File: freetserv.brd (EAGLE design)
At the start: 91.4 x 82.5 mm, 72 parts, among them IC2 SN75240PW, Q1 12MHz, Q2 6MHz, U1 MCP16311-E/MS

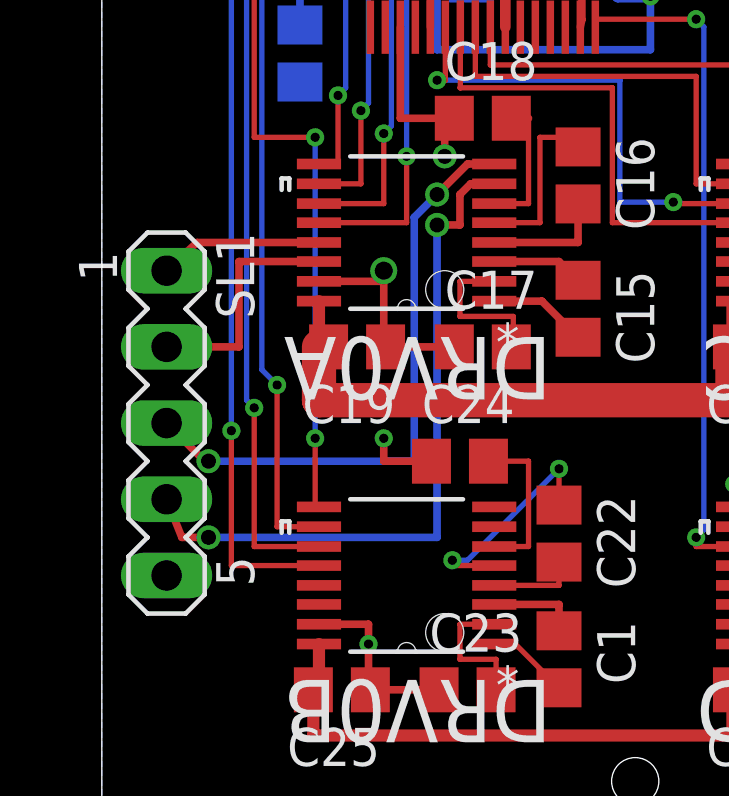
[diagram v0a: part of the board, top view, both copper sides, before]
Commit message: wire up a serial port
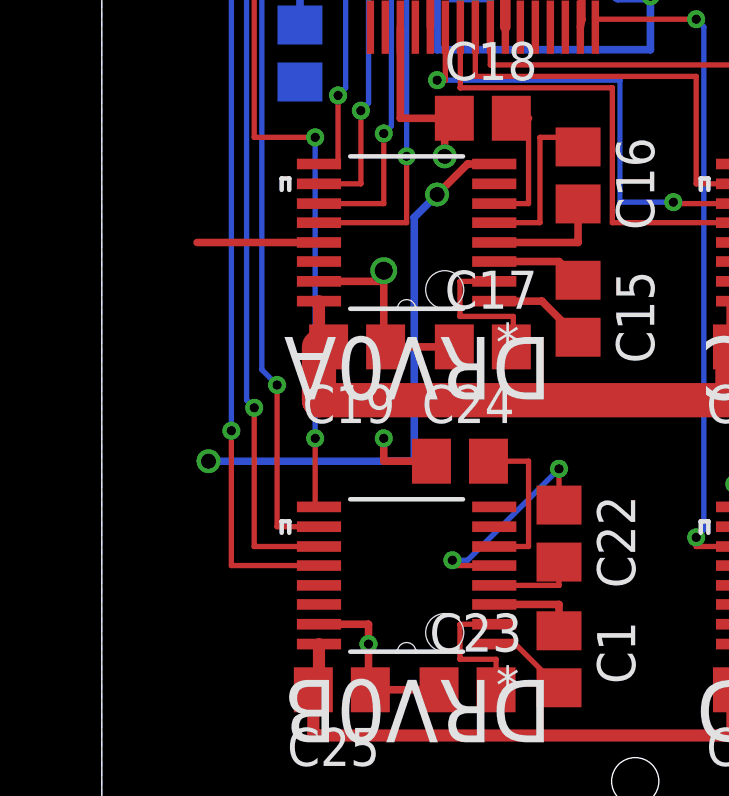
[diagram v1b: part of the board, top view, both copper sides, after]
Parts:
- removed SL1: (no value), con-lstb:MA05-1
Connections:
- removed net N$25: DRV0A.14, SL1.2
- removed net N$8: DRV0A.7, SL1.4
- new net N$37: DRV0A.14
- net GND: no longer SL1.5
- net N$19: no longer SL1.1
- net N$9: no longer SL1.3
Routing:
- net N$8: track 23.4 -> 0.00 mm, vias 2 -> 0
- net N$25: track 7.92 -> 0.00 mm
- net N$9: track 20.3 -> 18.5 mm
- net N$19: track 5.45 -> 4.06 mm
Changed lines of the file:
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@@
 <attribute name="PARTNO" value="1276-1003-1-ND" x="15.875" y="43.815" size="1.778" layer="27" rot="R270" display="off"/>
-</element>
-<element name="SL1" library="con-lstb" package="MA05-1" value="" x="2.159" y="35.56" rot="R270">
-<attribute name="MF" value="" x="2.159" y="35.56" size="1.778" layer="27" rot="R270" display="off"/>
-<attribute name="OC_FARNELL" value="unknown" x="2.159" y="35.56" size="1.778" layer="27" rot="R270" display="off"/>
-<attribute name="OC_NEWARK" value="unknown" x="2.159" y="35.56" size="1.778" layer="27" rot="R270" display="off"/>
-<attribute name="MPN" value="" x="2.159" y="35.56" size="1.778" layer="27" rot="R270" display="off"/>
 </element>
 <element name="C17" library="resistor" package="C0805" value="0.1uF" x="12.7" y="38.1">
@@
 <contactref element="C6" pad="2"/>
 <contactref element="C7" pad="2"/>
-<contactref element="SL1" pad="5"/>
 <polygon width="0.4064" layer="16">
 <vertex x="0" y="82.55"/>
@@
 <signal name="N$19">
 <contactref element="DRV0A" pad="13"/>
-<contactref element="SL1" pad="1"/>
 <wire x1="7.239" y1="41.5798" x2="3.175" y2="41.5798" width="0.254" layer="1"/>
-<wire x1="3.175" y1="41.5798" x2="2.159" y2="40.64" width="0.254" layer="1"/>
 </signal>
 <signal name="+3V3" class="2">
@@
 <wire x1="8.592" y1="57.36" x2="8.636" y2="57.404" width="0.1778" layer="1"/>
 </signal>
-<signal name="N$8">
-<contactref element="DRV0A" pad="7"/>
-<contactref element="SL1" pad="4"/>
-<wire x1="13.081" y1="43.5356" x2="12.2936" y2="43.5356" width="0.254" layer="1"/>
-<via x="11.176" y="42.164" extent="1-16" drill="0.5"/>
-<wire x1="11.176" y1="42.164" x2="11.176" y2="31.75" width="0.254" layer="16"/>
-<wire x1="11.176" y1="31.75" x2="3.556" y2="31.75" width="0.254" layer="16"/>
-<via x="3.556" y="31.75" extent="1-16" drill="0.5"/>
-<wire x1="3.556" y1="31.75" x2="2.667" y2="31.75" width="0.254" layer="1"/>
-<wire x1="2.667" y1="31.75" x2="2.159" y2="33.02" width="0.254" layer="1"/>
-<wire x1="12.2936" y1="43.5356" x2="11.938" y2="43.18" width="0.254" layer="1"/>
-<wire x1="11.938" y1="43.18" x2="11.938" y2="42.164" width="0.254" layer="1"/>
-<wire x1="11.938" y1="42.164" x2="11.176" y2="42.164" width="0.254" layer="1"/>
-</signal>
 <signal name="N$9">
 <contactref element="DRV0A" pad="8"/>
 <wire x1="13.081" y1="44.196" x2="12.192" y2="44.196" width="0.254" layer="1"/>
-<contactref element="SL1" pad="3"/>
 <wire x1="12.192" y1="44.196" x2="11.176" y2="43.18" width="0.254" layer="1"/>
 <via x="11.176" y="43.18" extent="1-16" drill="0.5"/>
@@
 <via x="3.556" y="34.29" extent="1-16" drill="0.5"/>
 <wire x1="3.556" y1="34.29" x2="3.429" y2="34.29" width="0.254" layer="1"/>
-<wire x1="3.429" y1="34.29" x2="2.159" y2="35.56" width="0.254" layer="1"/>
 </signal>
 <signal name="N$10">
@@
 <wire x1="20.848" y1="53.36" x2="18.554" y2="53.36" width="0.1778" layer="1"/>
 </signal>
-<signal name="N$25">
-<contactref element="SL1" pad="2"/>
-<contactref element="DRV0A" pad="14"/>
-<wire x1="7.239" y1="40.9448" x2="4.572" y2="40.9448" width="0.254" layer="1"/>
-<wire x1="4.572" y1="40.9448" x2="4.572" y2="38.1" width="0.254" layer="1"/>
-<wire x1="4.572" y1="38.1" x2="2.159" y2="38.1" width="0.254" layer="1"/>
-</signal>
 <signal name="N$1">
 <contactref element="HUB0" pad="12"/>
@@
 <wire x1="52.07" y1="78.15" x2="52.07" y2="74.742" width="0.1778" layer="1"/>
 </signal>
+<signal name="N$37">
+<contactref element="DRV0A" pad="14"/>
+</signal>
 </signals>

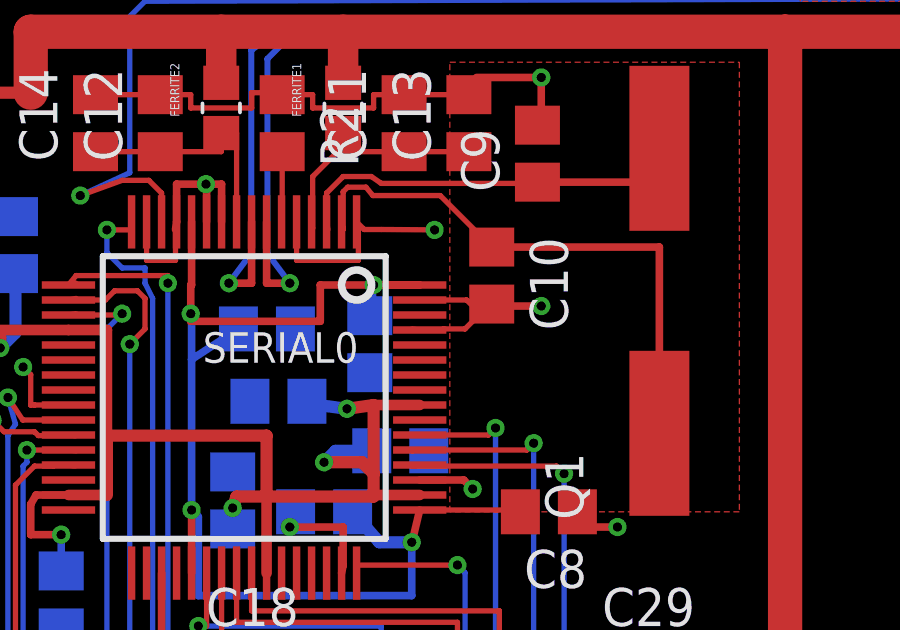
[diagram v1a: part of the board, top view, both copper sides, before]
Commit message: Bugfix: disconnect EEDATA/EECS from GND (Thanks Volker!)
With this fix, the FTDI converter is recognized by the host \o/
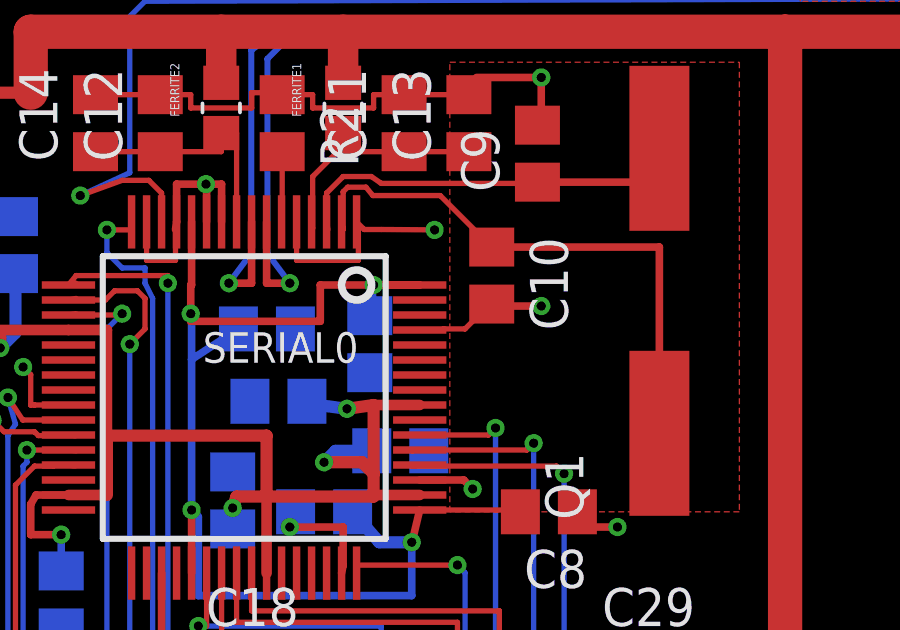
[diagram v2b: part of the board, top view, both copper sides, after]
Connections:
- net GND: no longer SERIAL0.61, SERIAL0.63
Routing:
- net GND: track 140.5 -> 137.3 mm
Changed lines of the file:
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@@
 <?xml version="1.0" encoding="utf-8"?>
 <!DOCTYPE eagle SYSTEM "eagle.dtd">
-<eagle version="7.3.0">
+<eagle version="7.4.0">
 <drawing>
 <settings>
@@
 <contactref element="C9" pad="2"/>
 <contactref element="C10" pad="2"/>
-<contactref element="SERIAL0" pad="63"/>
-<contactref element="SERIAL0" pad="61"/>
 <contactref element="C14" pad="2"/>
 <contactref element="C12" pad="2"/>
@@
 <wire x1="9.95" y1="48.756" x2="9.95" y2="45.72" width="0.254" layer="1"/>
 <wire x1="9.95" y1="45.72" x2="11.75" y2="45.72" width="0.254" layer="1"/>
-<wire x1="18.554" y1="56.86" x2="19.304" y2="56.86" width="0.1778" layer="1"/>
-<wire x1="18.3" y1="56.896" x2="18.554" y2="56.86" width="0.1778" layer="1"/>
 <via x="20.32" y="51.562" extent="1-16" drill="0.3048"/>
 <wire x1="20.32" y1="51.562" x2="20.022" y2="51.86" width="0.254" layer="1"/>
@@
 <wire x1="5.719" y1="54.36" x2="6.846" y2="54.36" width="0.1778" layer="1"/>
 <wire x1="20.955" y1="57.658" x2="20.828" y2="57.658" width="0.1778" layer="1"/>
-<wire x1="20.828" y1="57.658" x2="20.574" y2="57.404" width="0.1778" layer="1"/>
-<wire x1="20.574" y1="57.404" x2="20.066" y2="56.896" width="0.1778" layer="1"/>
-<wire x1="20.066" y1="56.896" x2="19.34" y2="56.896" width="0.1778" layer="1"/>
+<wire x1="20.828" y1="57.658" x2="20.066" y2="56.896" width="0.1778" layer="1"/>
 <wire x1="19.34" y1="56.896" x2="19.304" y2="56.86" width="0.1778" layer="1"/>
-<wire x1="18.554" y1="57.86" x2="20.118" y2="57.86" width="0.1778" layer="1"/>
-<wire x1="20.118" y1="57.86" x2="20.574" y2="57.404" width="0.1778" layer="1"/>
 <wire x1="17.272" y1="60.21" x2="16.704" y2="60.21" width="0.1778" layer="1"/>
 <wire x1="16.704" y1="60.21" x2="16.45" y2="60.464" width="0.1778" layer="1"/>
+<wire x1="20.066" y1="56.896" x2="19.34" y2="56.896" width="0.1778" layer="1"/>
 </signal>
 <signal name="USB0_DM_P">
